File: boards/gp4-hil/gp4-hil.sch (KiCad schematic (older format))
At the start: 0 parts

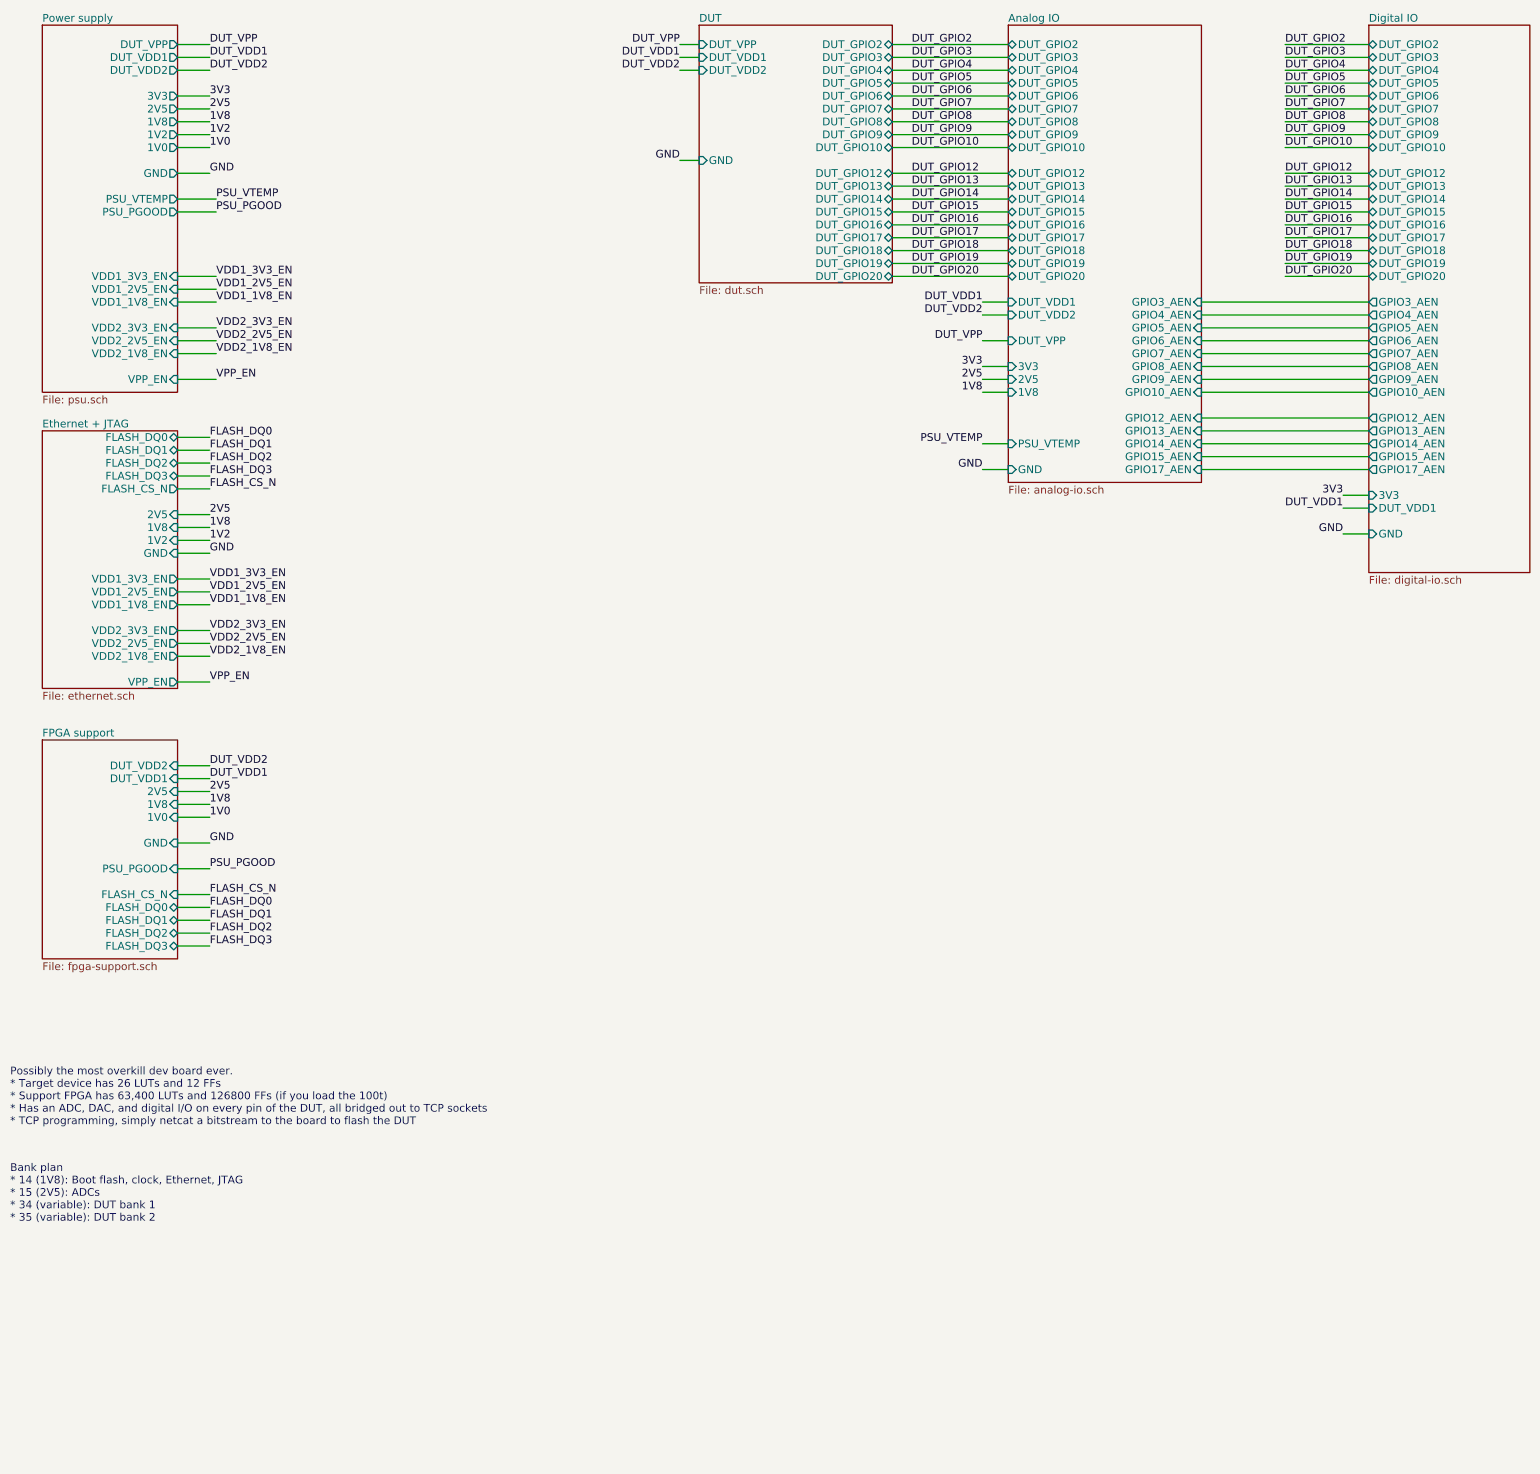
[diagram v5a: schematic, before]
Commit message: Added FPGA core clock, GPIO indicator LEDs, expansion header, lots of test points
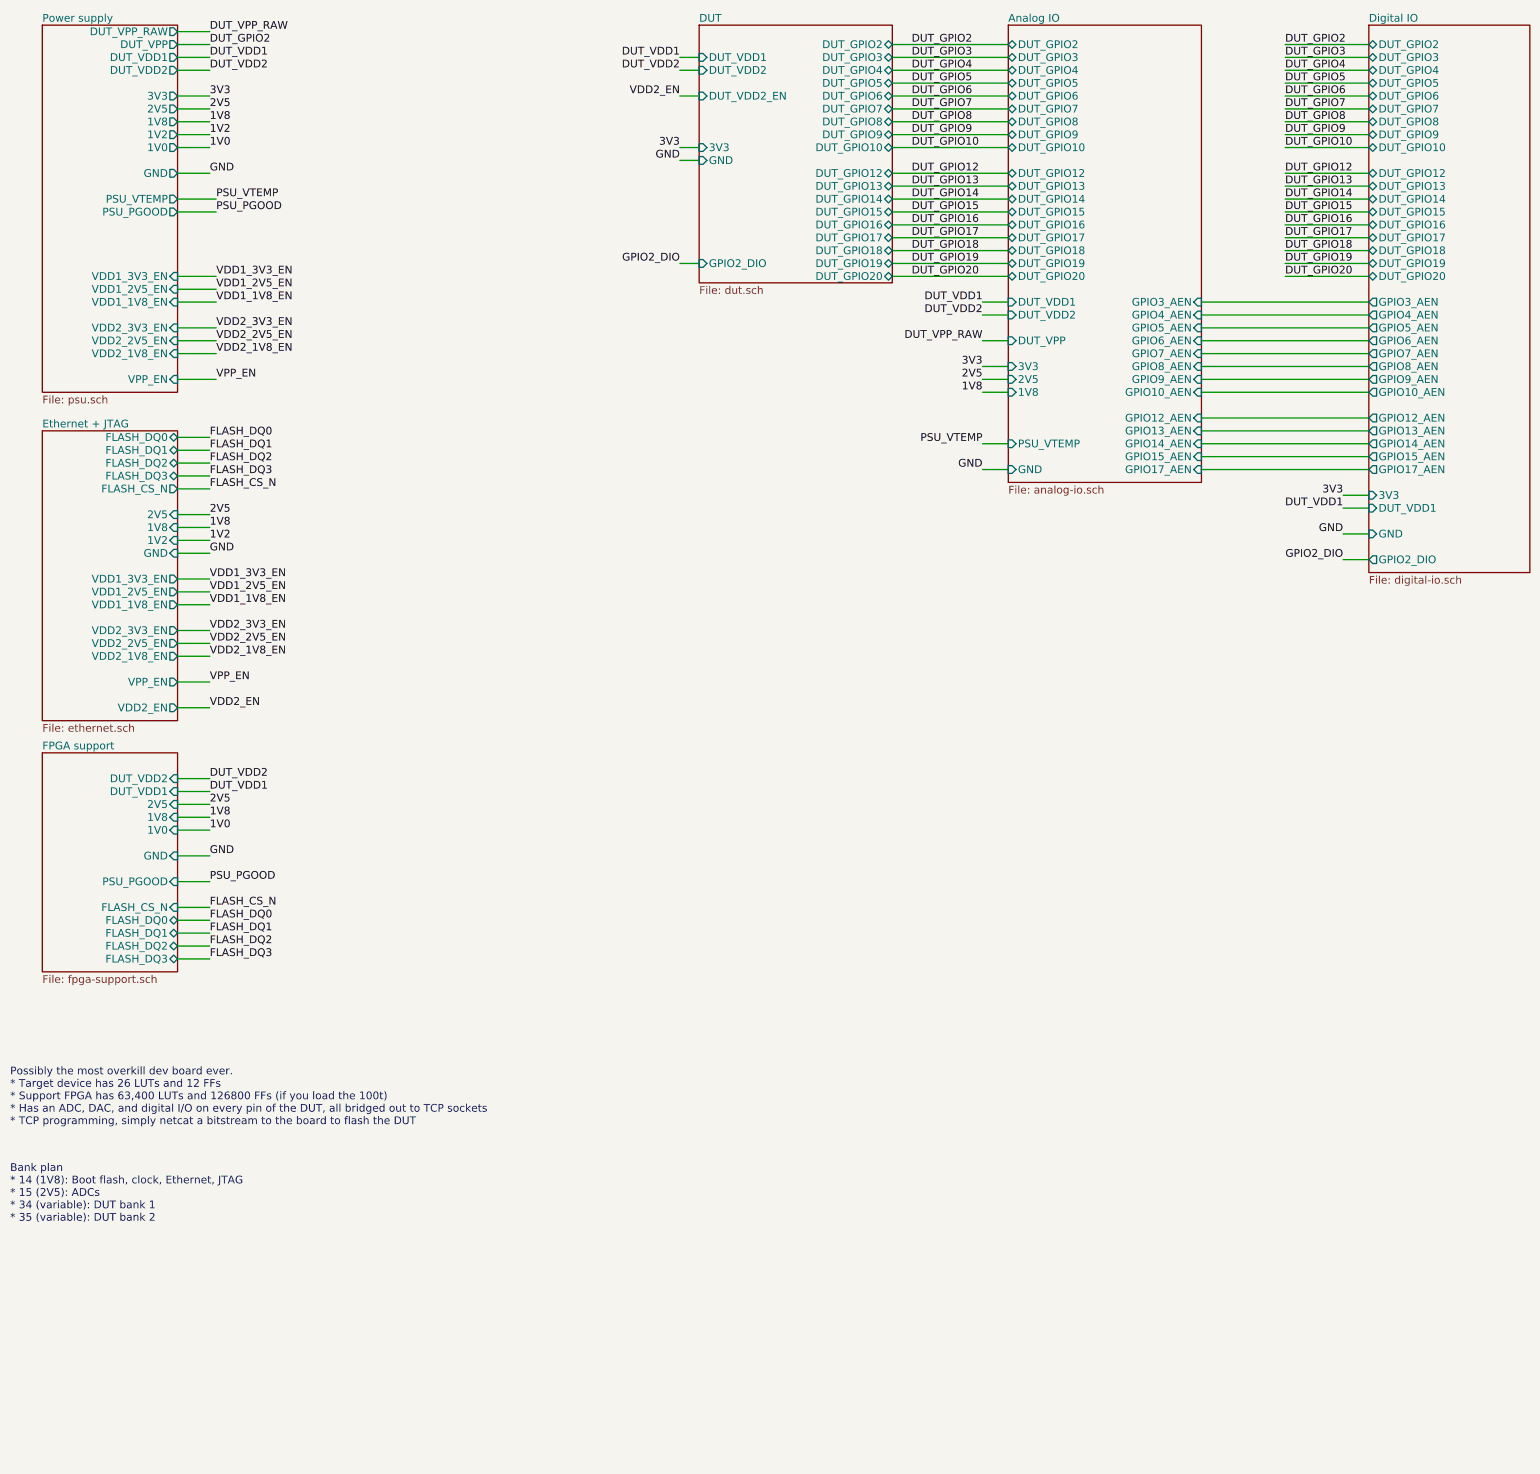
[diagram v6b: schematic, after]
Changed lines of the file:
@@
 F11 "PSU_VTEMP" O R 2550 2550 60
 F12 "PSU_PGOOD" O R 2550 2650 60
-F15 "VDD1_3V3_EN" I R 2550 3150 60
-F16 "VDD1_1V8_EN" I R 2550 3350 60
-F17 "VDD1_2V5_EN" I R 2550 3250 60
-F18 "VDD2_3V3_EN" I R 2550 3550 60
-F19 "VDD2_1V8_EN" I R 2550 3750 60
-F20 "VDD2_2V5_EN" I R 2550 3650 60
-F21 "VPP_EN" I R 2550 3950 60
+F13 "VDD1_3V3_EN" I R 2550 3150 60
+F14 "VDD1_1V8_EN" I R 2550 3350 60
+F15 "VDD1_2V5_EN" I R 2550 3250 60
+F16 "VDD2_3V3_EN" I R 2550 3550 60
+F17 "VDD2_1V8_EN" I R 2550 3750 60
+F18 "VDD2_2V5_EN" I R 2550 3650 60
+F19 "VPP_EN" I R 2550 3950 60
+F20 "DUT_VPP_RAW" O R 2550 1250 60
 $EndSheet
 $Sheet
-S 1500 4350 1050 2000
+S 1500 4350 1050 2250
 U 57316A40
 F0 "Ethernet + JTAG" 60
@@
 F16 "VDD2_1V8_EN" O R 2550 6100 60
 F17 "VPP_EN" O R 2550 6300 60
+F18 "VDD2_EN" O R 2550 6500 60
 $EndSheet
 $Sheet
@@
 F1 "dut.sch" 60
 F2 "DUT_VDD1" I L 6600 1450 60
-F3 "DUT_VPP" I L 6600 1350 60
-F4 "DUT_VDD2" I L 6600 1550 60
-F5 "GND" I L 6600 2250 60
-F6 "DUT_GPIO2" B R 8100 1350 60
-F7 "DUT_GPIO3" B R 8100 1450 60
-F8 "DUT_GPIO4" B R 8100 1550 60
-F9 "DUT_GPIO5" B R 8100 1650 60
-F10 "DUT_GPIO6" B R 8100 1750 60
-F11 "DUT_GPIO7" B R 8100 1850 60
-F12 "DUT_GPIO8" B R 8100 1950 60
-F13 "DUT_GPIO9" B R 8100 2050 60
-F14 "DUT_GPIO10" B R 8100 2150 60
-F15 "DUT_GPIO12" B R 8100 2350 60
-F16 "DUT_GPIO13" B R 8100 2450 60
-F17 "DUT_GPIO14" B R 8100 2550 60
-F18 "DUT_GPIO15" B R 8100 2650 60
-F19 "DUT_GPIO16" B R 8100 2750 60
-F20 "DUT_GPIO17" B R 8100 2850 60
-F21 "DUT_GPIO18" B R 8100 2950 60
-F22 "DUT_GPIO19" B R 8100 3050 60
-F23 "DUT_GPIO20" B R 8100 3150 60
+F3 "DUT_VDD2" I L 6600 1550 60
+F4 "GND" I L 6600 2250 60
+F5 "DUT_GPIO2" B R 8100 1350 60
+F6 "DUT_GPIO3" B R 8100 1450 60
+F7 "DUT_GPIO4" B R 8100 1550 60
+F8 "DUT_GPIO5" B R 8100 1650 60
+F9 "DUT_GPIO6" B R 8100 1750 60
+F10 "DUT_GPIO7" B R 8100 1850 60
+F11 "DUT_GPIO8" B R 8100 1950 60
+F12 "DUT_GPIO9" B R 8100 2050 60
+F13 "DUT_GPIO10" B R 8100 2150 60
+F14 "DUT_GPIO12" B R 8100 2350 60
+F15 "DUT_GPIO13" B R 8100 2450 60
+F16 "DUT_GPIO14" B R 8100 2550 60
+F17 "DUT_GPIO15" B R 8100 2650 60
+F18 "DUT_GPIO16" B R 8100 2750 60
+F19 "DUT_GPIO17" B R 8100 2850 60
+F20 "DUT_GPIO18" B R 8100 2950 60
+F21 "DUT_GPIO19" B R 8100 3050 60
+F22 "DUT_GPIO20" B R 8100 3150 60
+F23 "DUT_VDD2_EN" I L 6600 1750 60
+F24 "GPIO2_DIO" I L 6600 3050 60
+F25 "3V3" I L 6600 2150 60
 $EndSheet
 $Sheet
@@
 $EndSheet
 $Sheet
-S 1500 6750 1050 1700
+S 1500 6850 1050 1700
 U 57316B0C
 F0 "FPGA support" 60
 F1 "fpga-support.sch" 60
-F2 "GND" I R 2550 7550 60
-F3 "1V0" I R 2550 7350 60
-F4 "1V8" I R 2550 7250 60
-F5 "2V5" I R 2550 7150 60
-F6 "DUT_VDD1" I R 2550 7050 60
-F7 "DUT_VDD2" I R 2550 6950 60
-F8 "PSU_PGOOD" I R 2550 7750 60
-F9 "FLASH_CS_N" I R 2550 7950 60
-F10 "FLASH_DQ0" B R 2550 8050 60
-F11 "FLASH_DQ1" B R 2550 8150 60
-F12 "FLASH_DQ2" B R 2550 8250 60
-F13 "FLASH_DQ3" B R 2550 8350 60
+F2 "GND" I R 2550 7650 60
+F3 "1V0" I R 2550 7450 60
+F4 "1V8" I R 2550 7350 60
+F5 "2V5" I R 2550 7250 60
+F6 "DUT_VDD1" I R 2550 7150 60
+F7 "DUT_VDD2" I R 2550 7050 60
+F8 "PSU_PGOOD" I R 2550 7850 60
+F9 "FLASH_CS_N" I R 2550 8050 60
+F10 "FLASH_DQ0" B R 2550 8150 60
+F11 "FLASH_DQ1" B R 2550 8250 60
+F12 "FLASH_DQ2" B R 2550 8350 60
+F13 "FLASH_DQ3" B R 2550 8450 60
 $EndSheet
 Text Notes 1250 10500 0    60   ~ 0
@@
 F34 "GPIO15_AEN" O L 11800 4550 60
 F35 "GPIO17_AEN" O L 11800 4650 60
+F36 "GPIO2_DIO" O L 11800 5350 60
 $EndSheet
 Text Label 11150 1350 0    60   ~ 0
@@
 Text Label 8800 4450 2    60   ~ 0
 PSU_VTEMP
-Text Label 2800 1350 0    60   ~ 0
-DUT_VPP
 Text Label 2800 1450 0    60   ~ 0
 DUT_VDD1
-Text Label 2800 1550 0    60   ~ 0
-DUT_VDD2
 Text Label 2800 1750 0    60   ~ 0
 3V3
@@
 Text Label 2800 2350 0    60   ~ 0
 GND
-Text Label 6450 1350 2    60   ~ 0
-DUT_VPP
 Text Label 6450 1450 2    60   ~ 0
 DUT_VDD1
-Text Label 6450 1550 2    60   ~ 0
-DUT_VDD2
 Text Label 6450 2250 2    60   ~ 0
 GND
@@
 	6450 2250 6600 2250
 Wire Wire Line
-	6450 1550 6600 1550
-Wire Wire Line
 	6450 1450 6600 1450
-Wire Wire Line
-	6450 1350 6600 1350
 Wire Wire Line
 	2800 5300 2550 5300
@@
 	8800 4050 9000 4050
 Text Label 8800 3650 2    60   ~ 0
-DUT_VPP
+DUT_VPP_RAW
 Wire Wire Line
 	8800 3650 9000 3650
@@
 Wire Wire Line
 	8800 3350 9000 3350
-Text Label 8800 3450 2    60   ~ 0
-DUT_VDD2
-Wire Wire Line
-	8800 3450 9000 3450
 Text Label 11600 4850 2    60   ~ 0
 3V3
@@
 Wire Wire Line
 	2850 2550 2550 2550
-Text Label 2800 6950 0    60   ~ 0
-DUT_VDD2
-Wire Wire Line
-	2800 6950 2550 6950
-Text Label 2800 7050 0    60   ~ 0
+Wire Wire Line
+	2800 7050 2550 7050
+Text Label 2800 7150 0    60   ~ 0
 DUT_VDD1
 Wire Wire Line
-	2550 7050 2800 7050
-Text Label 2800 7150 0    60   ~ 0
+	2550 7150 2800 7150
+Text Label 2800 7250 0    60   ~ 0
 2V5
-Wire Wire Line
-	2800 7150 2550 7150
-Text Label 2800 7250 0    60   ~ 0
-1V8
 Wire Wire Line
 	2800 7250 2550 7250
 Text Label 2800 7350 0    60   ~ 0
+1V8
+Wire Wire Line
+	2800 7350 2550 7350
+Text Label 2800 7450 0    60   ~ 0
 1V0
 Wire Wire Line
-	2800 7350 2550 7350
-Text Label 2800 7550 0    60   ~ 0
+	2800 7450 2550 7450
+Text Label 2800 7650 0    60   ~ 0
 GND
 Wire Wire Line
-	2800 7550 2550 7550
-Text Label 2800 7750 0    60   ~ 0
+	2800 7650 2550 7650
+Text Label 2800 7850 0    60   ~ 0
 PSU_PGOOD
 Wire Wire Line
-	2800 7750 2550 7750
-Text Label 2800 8050 0    60   ~ 0
+	2800 7850 2550 7850
+Text Label 2800 8150 0    60   ~ 0
 FLASH_DQ0
-Wire Wire Line
-	2800 7950 2550 7950
-Text Label 2800 8150 0    60   ~ 0
-FLASH_DQ1
 Wire Wire Line
 	2800 8050 2550 8050
 Text Label 2800 8250 0    60   ~ 0
-FLASH_DQ2
+FLASH_DQ1
 Wire Wire Line
 	2800 8150 2550 8150
 Text Label 2800 8350 0    60   ~ 0
+FLASH_DQ2
+Wire Wire Line
+	2800 8250 2550 8250
+Text Label 2800 8450 0    60   ~ 0
 FLASH_DQ3
 Wire Wire Line
-	2800 8250 2550 8250
-Text Label 2800 7950 0    60   ~ 0
+	2800 8350 2550 8350
+Text Label 2800 8050 0    60   ~ 0
 FLASH_CS_N
 Wire Wire Line
-	2800 8350 2550 8350
+	2800 8450 2550 8450
 Text Label 2850 2650 0    60   ~ 0
 PSU_PGOOD
@@
 Wire Wire Line
 	11800 4250 10500 4250
+Text Label 2800 1350 0    60   ~ 0
+DUT_GPIO2
+Text Label 2800 7050 0    60   ~ 0
+DUT_VDD2
+Wire Wire Line
+	8800 3450 9000 3450
+Text Label 8800 3450 2    60   ~ 0
+DUT_VDD2
+Wire Wire Line
+	6450 1550 6600 1550
+Text Label 6450 1550 2    60   ~ 0
+DUT_VDD2
+Text Label 2800 1550 0    60   ~ 0
+DUT_VDD2
+Text Label 2800 6500 0    60   ~ 0
+VDD2_EN
+Wire Wire Line
+	2800 6500 2550 6500
+Text Label 6450 1750 2    60   ~ 0
+VDD2_EN
+Wire Wire Line
+	6450 1750 6600 1750
+Text Label 2800 1250 0    60   ~ 0
+DUT_VPP_RAW
+Wire Wire Line
+	2800 1250 2550 1250
+Text Label 11600 5350 2    60   ~ 0
+GPIO2_DIO
+Wire Wire Line
+	11600 5350 11800 5350
+Text Label 6450 3050 2    60   ~ 0
+GPIO2_DIO
+Wire Wire Line
+	6450 3050 6600 3050
+Text Label 6450 2150 2    60   ~ 0
+3V3
+Wire Wire Line
+	6450 2150 6600 2150
 $EndSCHEMATC

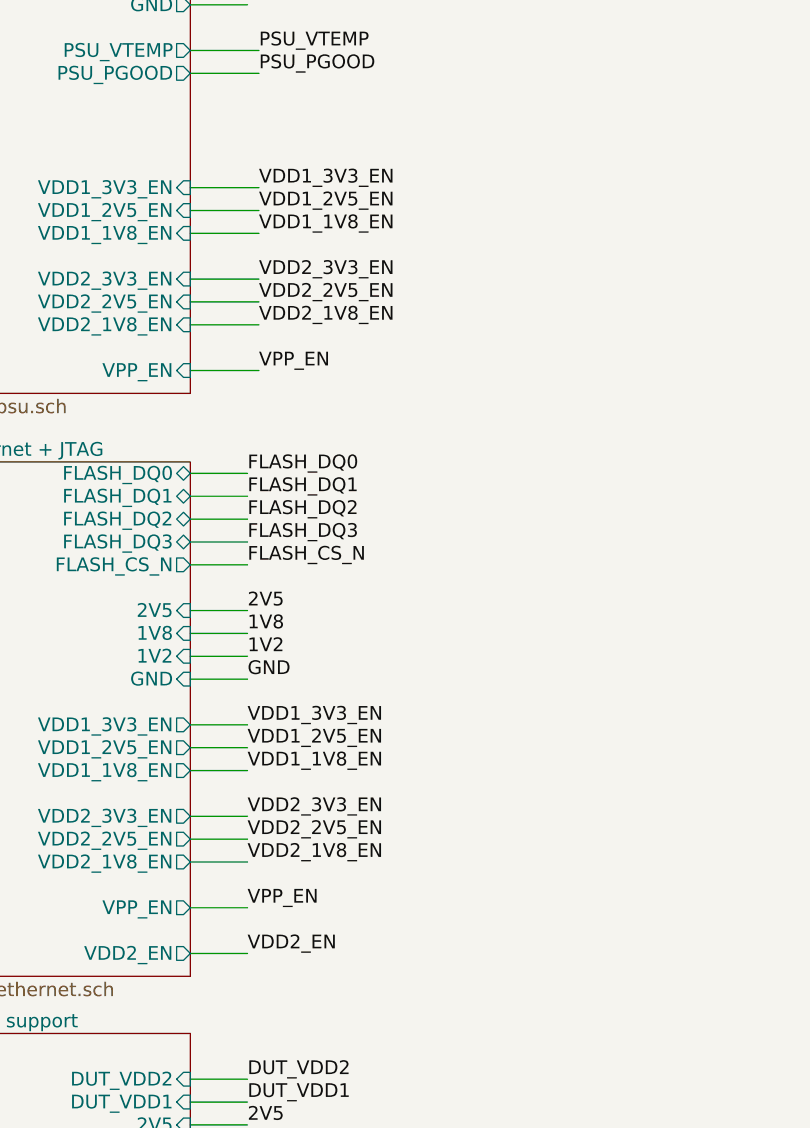
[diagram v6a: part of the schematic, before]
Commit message: Added a bunch of pullups/downs
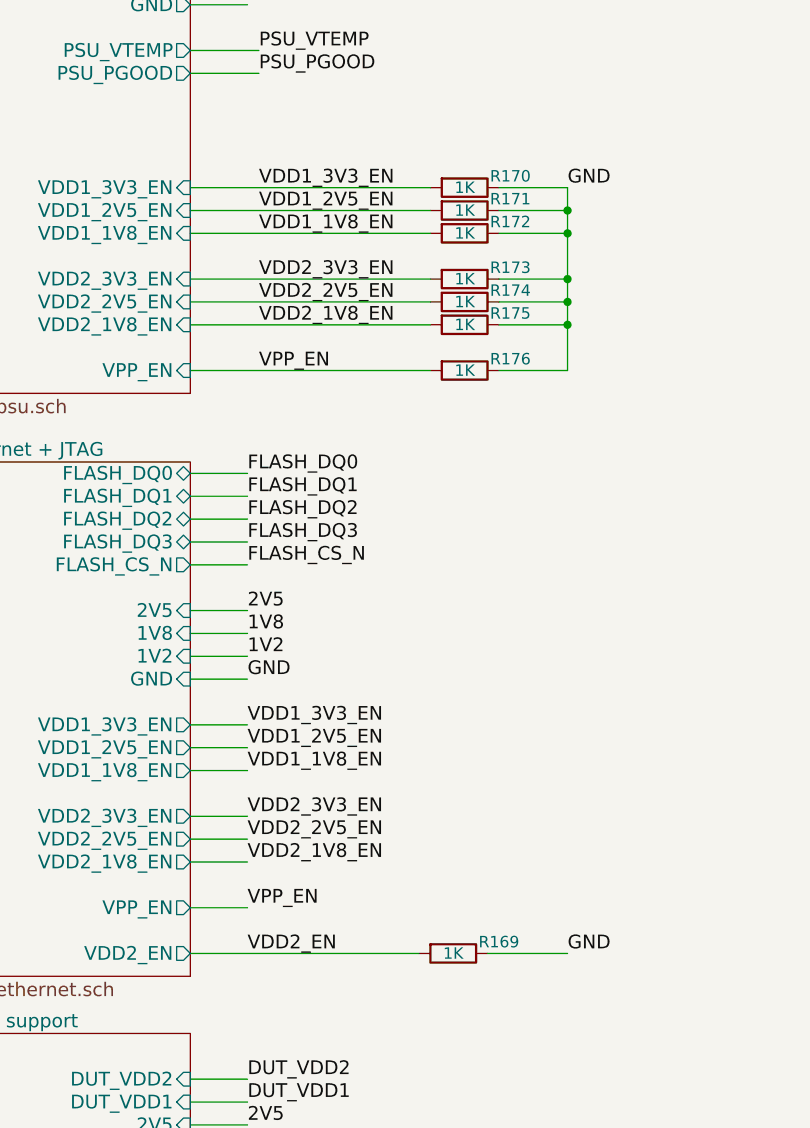
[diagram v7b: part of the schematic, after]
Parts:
- added R169, R170, R171, R172, R173, R174, R175, R176: 1K, symbol R
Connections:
- net GND: now also R169.1, R170.1, R171.1, R172.1, R173.1, R174.1, R175.1, R176.1
- net VDD1_1V8_EN: now also R172.2
- net VDD1_2V5_EN: now also R171.2
- net VDD1_3V3_EN: now also R170.2
- net VDD2_1V8_EN: now also R175.2
- net VDD2_2V5_EN: now also R174.2
- net VDD2_3V3_EN: now also R173.2
- net VDD2_EN: now also R169.2
- net VPP_EN: now also R176.2
